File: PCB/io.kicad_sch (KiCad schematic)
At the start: 15 parts, among them SW3 Handswitch W LED, U9 OLED_Waveshare

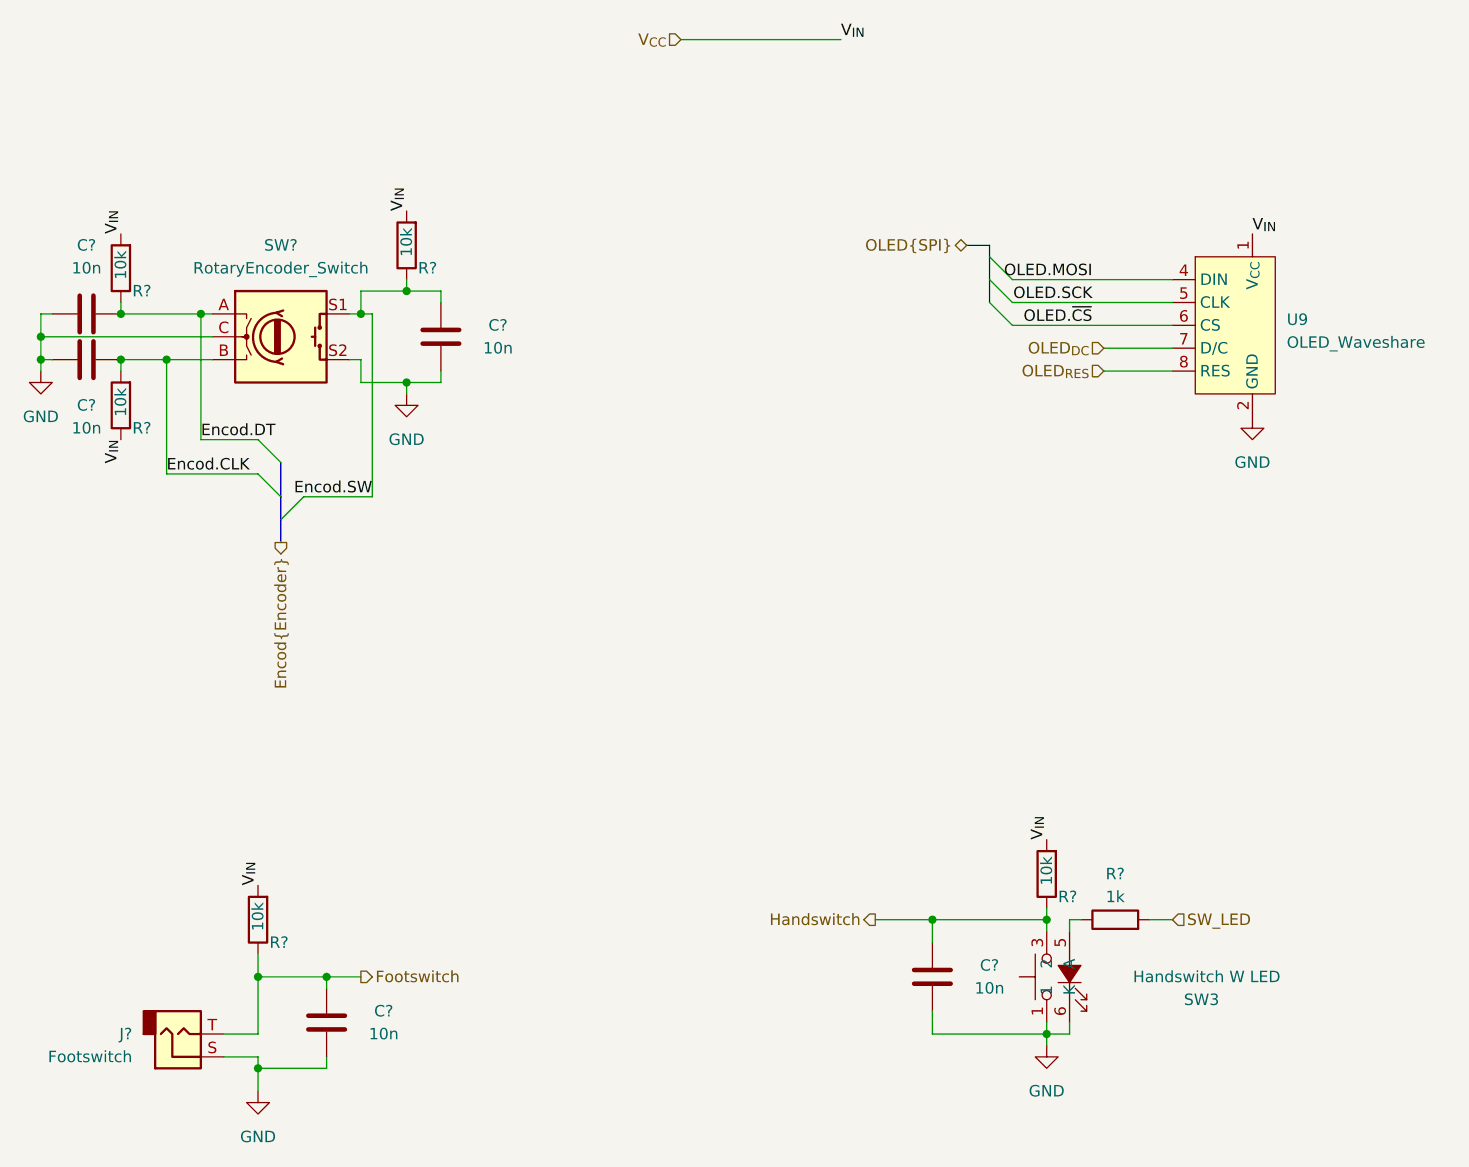
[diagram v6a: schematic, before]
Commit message: switch kicad 8 and change USB connector
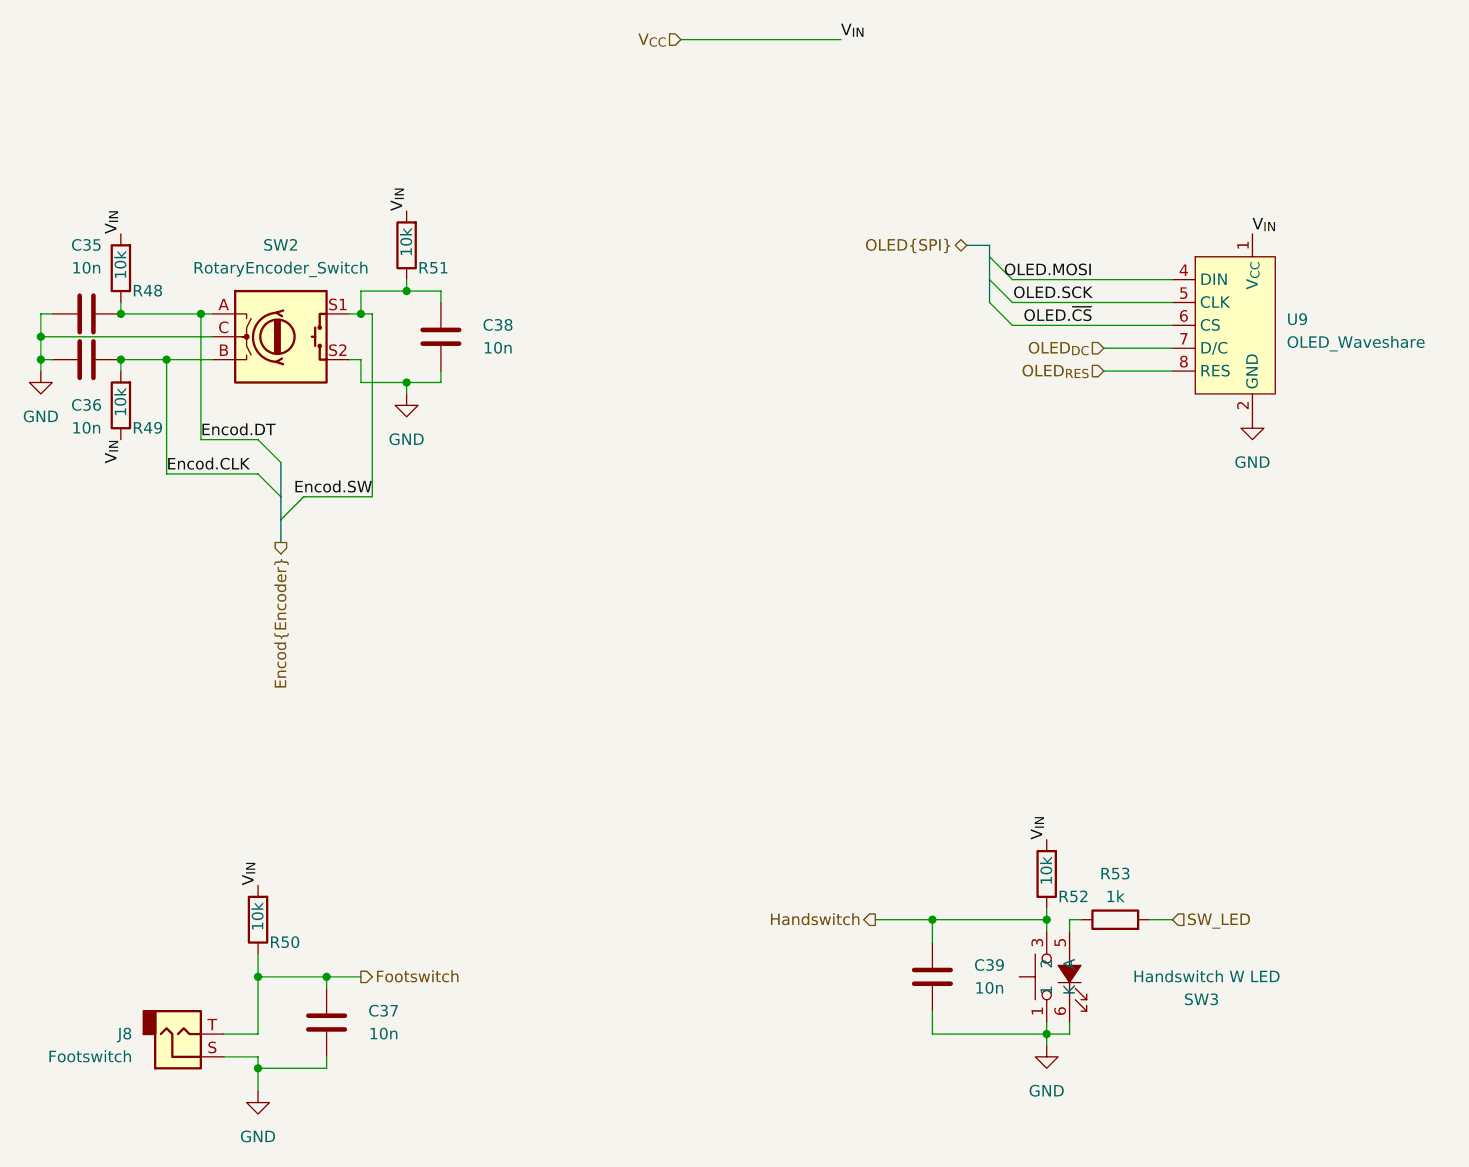
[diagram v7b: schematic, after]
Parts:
- gave numbers to parts that had none: 13
